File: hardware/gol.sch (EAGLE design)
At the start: 68 parts, among them J1 TC2050-IDC, J2 2057-MCR-B-S-RA-TSMT-NP-CS4-T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, U1 STM32F072CBT, U2 AP2111H-3.3TRG1SOT-223_DIO-M

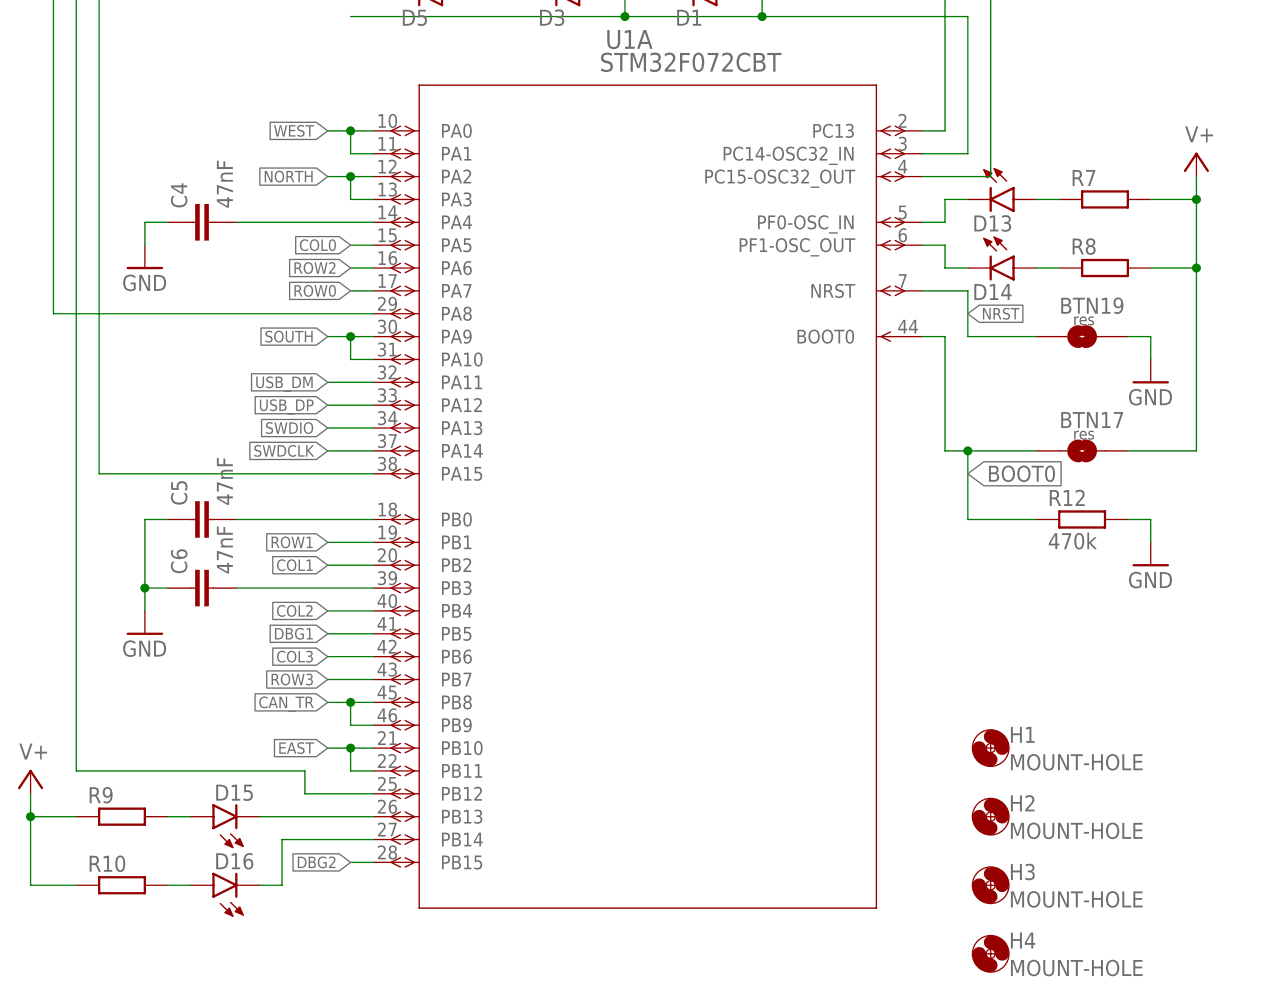
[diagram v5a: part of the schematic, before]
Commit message: Moves D15/16 to a two-way charlieplexing.
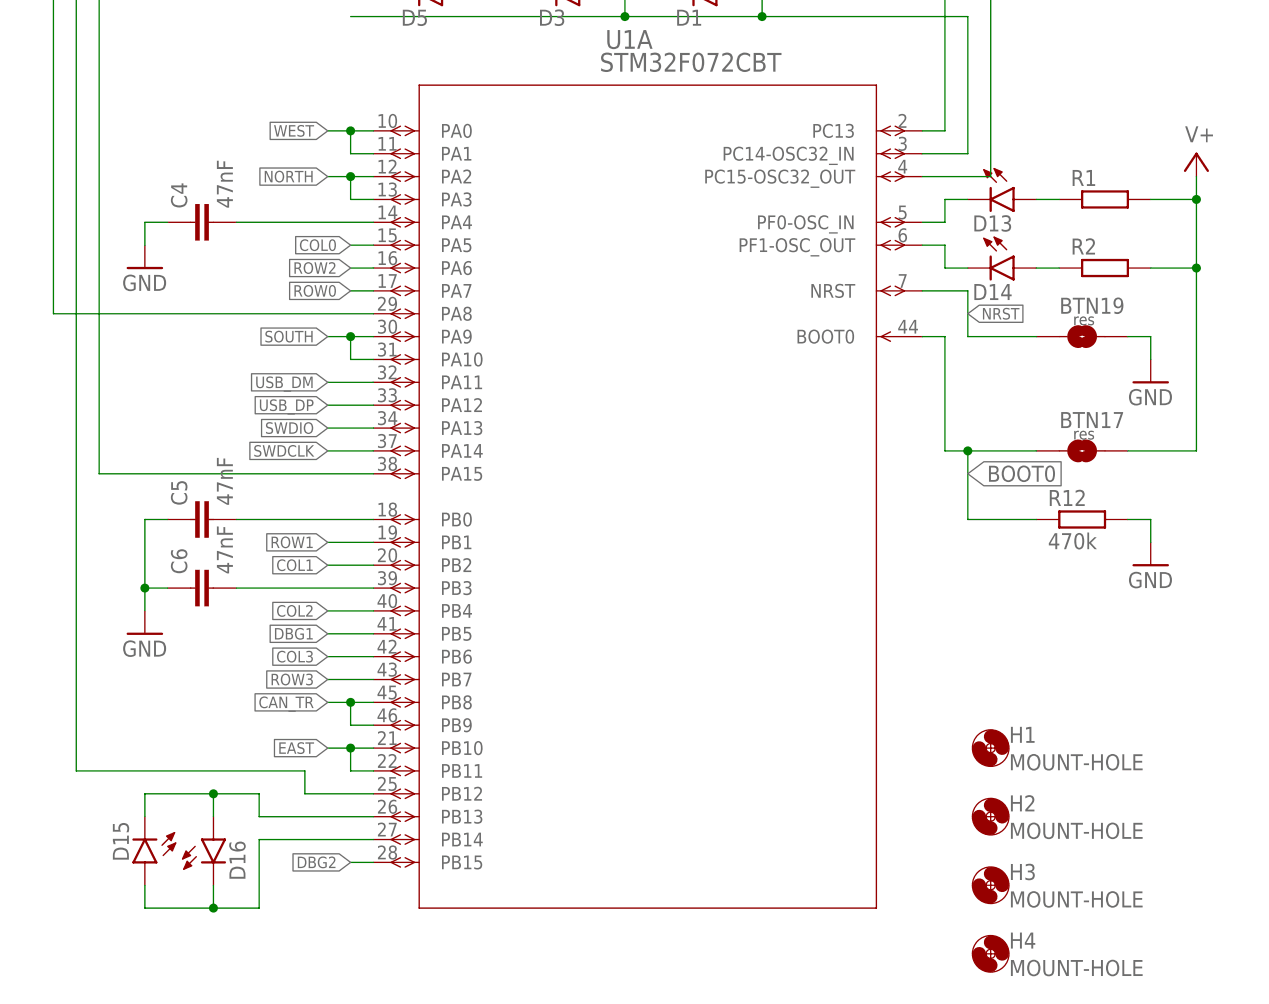
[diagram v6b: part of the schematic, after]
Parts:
- removed R10, R9: R-EU-0207/8, parts:R-EU-0207/8
- renumbered R7 to R1, R8 to R2
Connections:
- removed net N$22: D15.A, R9.2
- removed net N$23: D16.A, R10.2
- net OUTD15: now also D16.A
- net OUTD16: now also D15.A
- net V+: no longer R10.1, R9.1
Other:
- moved on the sheet: D15, D16
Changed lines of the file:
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@@
 <part name="SUPPLY2" library="supply2" library_urn="urn:adsk.eagle:library:372" deviceset="V+" device=""/>
 <part name="GND2" library="supply1" library_urn="urn:adsk.eagle:library:371" deviceset="GND" device=""/>
-<part name="R7" library="parts" deviceset="R-EU-0207/8" device=""/>
-<part name="R8" library="parts" deviceset="R-EU-0207/8" device=""/>
-<part name="R9" library="parts" deviceset="R-EU-0207/8" device=""/>
-<part name="R10" library="parts" deviceset="R-EU-0207/8" device=""/>
+<part name="R1" library="parts" deviceset="R-EU-0207/8" device=""/>
+<part name="R2" library="parts" deviceset="R-EU-0207/8" device=""/>
 <part name="SOUTH" library="pinhead" library_urn="urn:adsk.eagle:library:325" deviceset="PINHD-1X4" device="/90" package3d_urn="urn:adsk.eagle:package:22404/2" value="SOUTH"/>
 <part name="NORTH" library="parts" deviceset="PINHD-1X04" device="1X04-RA-FEM" value="NORTH"/>
@@
 <part name="D15" library="parts" deviceset="LED-5MM" device=""/>
 <part name="D16" library="parts" deviceset="LED-5MM" device=""/>
-<part name="SUPPLY4" library="supply2" library_urn="urn:adsk.eagle:library:372" deviceset="V+" device=""/>
 <part name="R12" library="rcl" library_urn="urn:adsk.eagle:library:334" deviceset="R-EU_" device="R0603" package3d_urn="urn:adsk.eagle:package:23555/3" value="470k"/>
 <part name="GND6" library="supply1" library_urn="urn:adsk.eagle:library:371" deviceset="GND" device=""/>
@@
 <attribute name="VALUE" x="226.06" y="137.16" size="1.778" layer="96"/>
 </instance>
-<instance part="R7" gate="G$1" x="127" y="93.98" smashed="yes">
+<instance part="R1" gate="G$1" x="127" y="93.98" smashed="yes">
 <attribute name="NAME" x="123.19" y="95.4786" size="1.778" layer="95"/>
 </instance>
-<instance part="R8" gate="G$1" x="127" y="86.36" smashed="yes">
+<instance part="R2" gate="G$1" x="127" y="86.36" smashed="yes">
 <attribute name="NAME" x="123.19" y="87.8586" size="1.778" layer="95"/>
-</instance>
-<instance part="R9" gate="G$1" x="17.78" y="25.4" smashed="yes">
-<attribute name="NAME" x="13.97" y="26.8986" size="1.778" layer="95"/>
-</instance>
-<instance part="R10" gate="G$1" x="17.78" y="17.78" smashed="yes">
-<attribute name="NAME" x="13.97" y="19.2786" size="1.778" layer="95"/>
 </instance>
 <instance part="SOUTH" gate="A" x="48.26" y="157.48" smashed="yes" rot="MR180">
@@
 <attribute name="NAME" x="112.268" y="82.804" size="1.778" layer="95"/>
 </instance>
-<instance part="D15" gate="G$1" x="27.94" y="25.4" smashed="yes" rot="R90">
-<attribute name="NAME" x="32.512" y="28.956" size="1.778" layer="95" rot="R180"/>
-</instance>
-<instance part="D16" gate="G$1" x="27.94" y="17.78" smashed="yes" rot="R90">
-<attribute name="NAME" x="32.512" y="21.336" size="1.778" layer="95" rot="R180"/>
-</instance>
-<instance part="SUPPLY4" gate="1" x="7.62" y="30.48" smashed="yes">
-<attribute name="VALUE" x="6.35" y="31.75" size="1.778" layer="96"/>
+<instance part="D15" gate="G$1" x="20.32" y="20.32" smashed="yes" rot="R180">
+<attribute name="NAME" x="16.764" y="24.892" size="1.778" layer="95" rot="R270"/>
+</instance>
+<instance part="D16" gate="G$1" x="27.94" y="22.86" smashed="yes">
+<attribute name="NAME" x="31.496" y="18.288" size="1.778" layer="95" rot="R90"/>
 </instance>
 <instance part="R12" gate="G$1" x="124.46" y="58.42" smashed="yes">
@@
 </segment>
 <segment>
-<pinref part="R7" gate="G$1" pin="2"/>
+<pinref part="R1" gate="G$1" pin="2"/>
 <wire x1="132.08" y1="93.98" x2="137.16" y2="93.98" width="0.1524" layer="91"/>
 <wire x1="137.16" y1="93.98" x2="137.16" y2="86.36" width="0.1524" layer="91"/>
-<pinref part="R8" gate="G$1" pin="2"/>
+<pinref part="R2" gate="G$1" pin="2"/>
 <wire x1="132.08" y1="86.36" x2="137.16" y2="86.36" width="0.1524" layer="91"/>
 <junction x="137.16" y="86.36"/>
@@
 <wire x1="137.16" y1="93.98" x2="137.16" y2="96.52" width="0.1524" layer="91"/>
 <junction x="137.16" y="93.98"/>
-</segment>
-<segment>
-<pinref part="R9" gate="G$1" pin="1"/>
-<wire x1="12.7" y1="25.4" x2="7.62" y2="25.4" width="0.1524" layer="91"/>
-<pinref part="SUPPLY4" gate="1" pin="V+"/>
-<wire x1="7.62" y1="25.4" x2="7.62" y2="27.94" width="0.1524" layer="91"/>
-<pinref part="R10" gate="G$1" pin="1"/>
-<wire x1="12.7" y1="17.78" x2="7.62" y2="17.78" width="0.1524" layer="91"/>
-<wire x1="7.62" y1="17.78" x2="7.62" y2="25.4" width="0.1524" layer="91"/>
-<junction x="7.62" y="25.4"/>
 </segment>
 <segment>
@@
 <segment>
 <pinref part="D13" gate="G$1" pin="A"/>
-<pinref part="R7" gate="G$1" pin="1"/>
+<pinref part="R1" gate="G$1" pin="1"/>
 <wire x1="119.38" y1="93.98" x2="121.92" y2="93.98" width="0.1524" layer="91"/>
 </segment>
@@
 <segment>
 <pinref part="D14" gate="G$1" pin="A"/>
-<pinref part="R8" gate="G$1" pin="1"/>
+<pinref part="R2" gate="G$1" pin="1"/>
 <wire x1="119.38" y1="86.36" x2="121.92" y2="86.36" width="0.1524" layer="91"/>
 </segment>
@@
 <pinref part="U1" gate="A" pin="PB13"/>
 <pinref part="D15" gate="G$1" pin="C"/>
-<wire x1="45.72" y1="25.4" x2="33.02" y2="25.4" width="0.1524" layer="91"/>
+<pinref part="D16" gate="G$1" pin="A"/>
+<wire x1="20.32" y1="27.94" x2="20.32" y2="25.4" width="0.1524" layer="91"/>
+<wire x1="20.32" y1="27.94" x2="27.94" y2="27.94" width="0.1524" layer="91"/>
+<wire x1="27.94" y1="27.94" x2="27.94" y2="25.4" width="0.1524" layer="91"/>
+<wire x1="27.94" y1="27.94" x2="33.02" y2="27.94" width="0.1524" layer="91"/>
+<junction x="27.94" y="27.94"/>
+<wire x1="33.02" y1="27.94" x2="33.02" y2="25.4" width="0.1524" layer="91"/>
+<wire x1="33.02" y1="25.4" x2="45.72" y2="25.4" width="0.1524" layer="91"/>
 </segment>
 </net>
@@
 <segment>
 <pinref part="U1" gate="A" pin="PB14"/>
-<wire x1="45.72" y1="22.86" x2="35.56" y2="22.86" width="0.1524" layer="91"/>
+<wire x1="45.72" y1="22.86" x2="33.02" y2="22.86" width="0.1524" layer="91"/>
 <pinref part="D16" gate="G$1" pin="C"/>
-<wire x1="35.56" y1="22.86" x2="35.56" y2="17.78" width="0.1524" layer="91"/>
-<wire x1="35.56" y1="17.78" x2="33.02" y2="17.78" width="0.1524" layer="91"/>
-</segment>
-</net>
-<net name="N$22" class="0">
-<segment>
+<wire x1="20.32" y1="15.24" x2="27.94" y2="15.24" width="0.1524" layer="91"/>
+<wire x1="27.94" y1="15.24" x2="27.94" y2="17.78" width="0.1524" layer="91"/>
 <pinref part="D15" gate="G$1" pin="A"/>
-<pinref part="R9" gate="G$1" pin="2"/>
-<wire x1="25.4" y1="25.4" x2="22.86" y2="25.4" width="0.1524" layer="91"/>
-</segment>
-</net>
-<net name="N$23" class="0">
-<segment>
-<pinref part="D16" gate="G$1" pin="A"/>
-<pinref part="R10" gate="G$1" pin="2"/>
-<wire x1="25.4" y1="17.78" x2="22.86" y2="17.78" width="0.1524" layer="91"/>
-</segment>
-</net>
+<wire x1="20.32" y1="17.78" x2="20.32" y2="15.24" width="0.1524" layer="91"/>
+<junction x="27.94" y="15.24"/>
+<wire x1="27.94" y1="15.24" x2="33.02" y2="15.24" width="0.1524" layer="91"/>
+<wire x1="33.02" y1="15.24" x2="33.02" y2="22.86" width="0.1524" layer="91"/>
+</segment>
+</net>

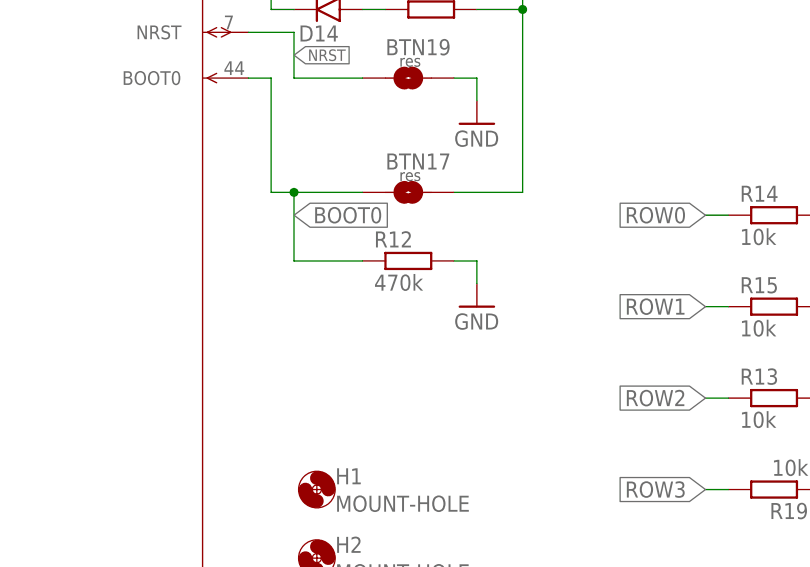
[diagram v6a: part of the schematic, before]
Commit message: Changes thickness of labels on the touch buttons.
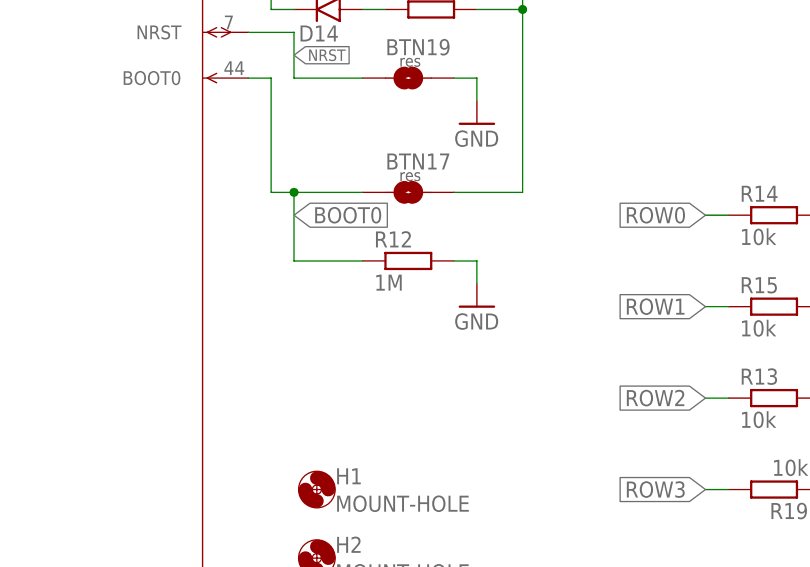
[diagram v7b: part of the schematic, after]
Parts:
- R12: value 470k -> 1M
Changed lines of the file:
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@@
 <part name="D15" library="parts" deviceset="LED-5MM" device=""/>
 <part name="D16" library="parts" deviceset="LED-5MM" device=""/>
-<part name="R12" library="rcl" library_urn="urn:adsk.eagle:library:334" deviceset="R-EU_" device="R0603" package3d_urn="urn:adsk.eagle:package:23555/3" value="470k"/>
+<part name="R12" library="rcl" library_urn="urn:adsk.eagle:library:334" deviceset="R-EU_" device="R0603" package3d_urn="urn:adsk.eagle:package:23555/3" value="1M"/>
 <part name="GND6" library="supply1" library_urn="urn:adsk.eagle:library:371" deviceset="GND" device=""/>
 <part name="BTN17" library="parts" deviceset="BUTTON-RES" device="" value="FLASH"/>
